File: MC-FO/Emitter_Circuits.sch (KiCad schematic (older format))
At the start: 9 parts, among them U27 74ACT08SCX, U28 IFE98

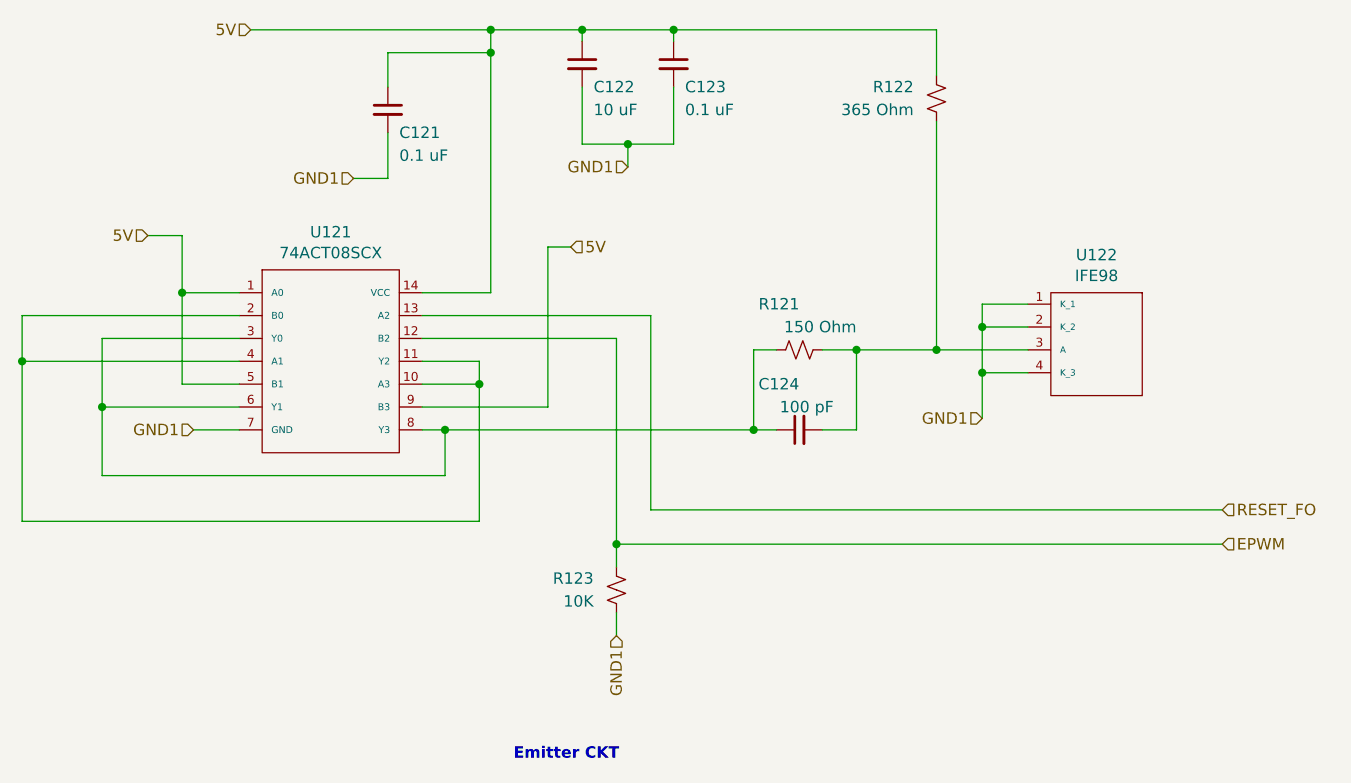
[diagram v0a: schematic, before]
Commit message: changed status1 to output of detector
reassigned footprint of 550 LED
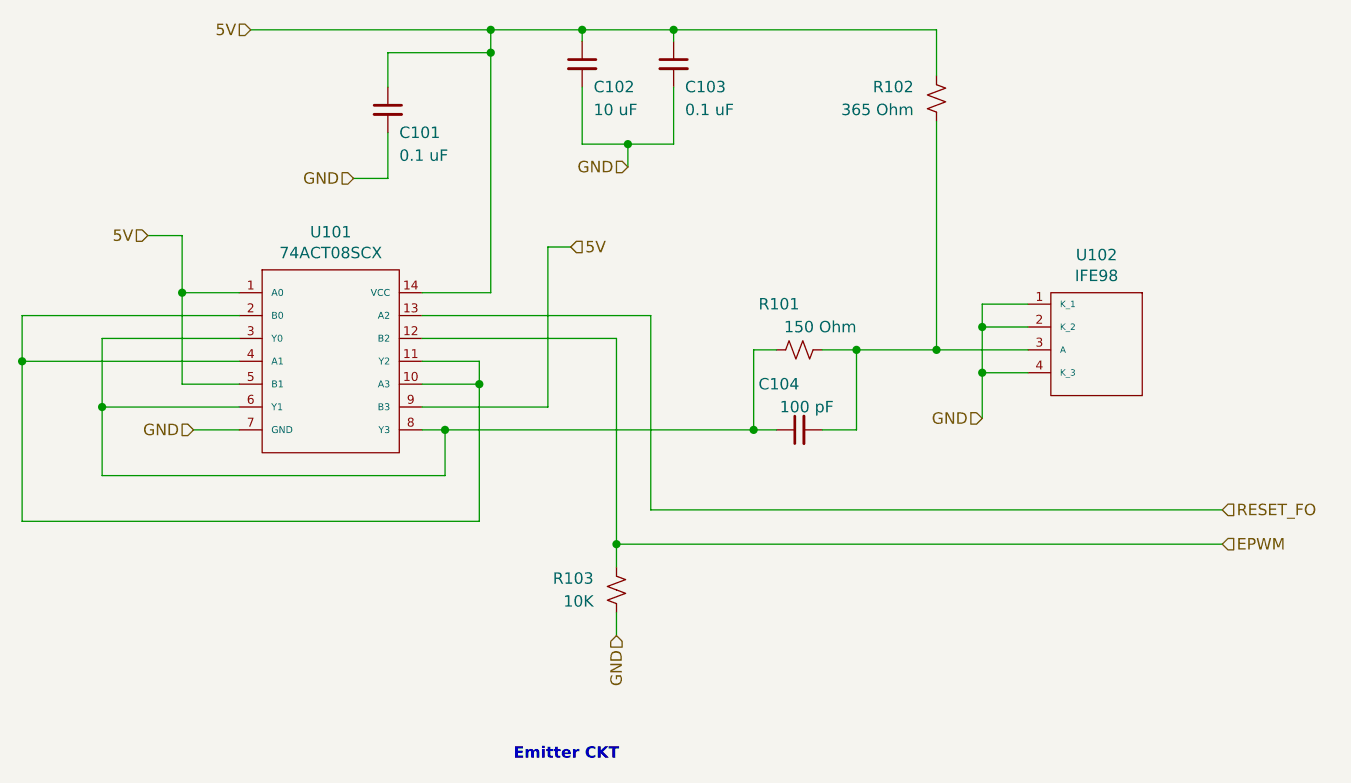
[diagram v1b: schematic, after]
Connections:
- net GND1 renamed GND
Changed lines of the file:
@@
 $Descr A4 11693 8268
 encoding utf-8
-Sheet 3 10
+Sheet 2 10
 Title ""
 Date ""
@@
 AR Path="/6176CA81/617428A7" Ref="R101"  Part="1"
 AR Path="/6176CAE4/617428A7" Ref="R121"  Part="1"
-F 0 "R121" V 6900 4400 50  0000 L CNN
+F 0 "R101" V 6900 4400 50  0000 L CNN
 F 1 "150 Ohm" V 6800 4150 50  0000 L CNN
 F 2 "Resistor_SMD:R_0603_1608Metric" H 6700 4400 50  0001 C CNN
@@
 AR Path="/6176CA81/61748E58" Ref="C104"  Part="1"
 AR Path="/6176CAE4/61748E58" Ref="C124"  Part="1"
-F 0 "C124" V 6900 4750 50  0000 L CNN
+F 0 "C104" V 6900 4750 50  0000 L CNN
 F 1 "100 pF" V 6800 4600 50  0000 L CNN
 F 2 "Capacitor_SMD:C_0603_1608Metric" H 6700 4750 50  0001 C CNN
@@
 AR Path="/6176CA81/6178E7F7" Ref="R102"  Part="1"
 AR Path="/6176CAE4/6178E7F7" Ref="R122"  Part="1"
-F 0 "R122" H 7400 3250 50  0000 L CNN
+F 0 "R102" H 7400 3250 50  0000 L CNN
 F 1 "365 Ohm" H 7400 3350 50  0000 L CNN
 F 2 "Resistor_SMD:R_0603_1608Metric" H 7300 3300 50  0001 C CNN
@@
 AR Path="/6176CA81/6171F0C9" Ref="C101"  Part="1"
 AR Path="/6176CAE4/6171F0C9" Ref="C121"  Part="1"
-F 0 "C121" H 4950 3250 50  0000 L CNN
+F 0 "C101" H 4950 3250 50  0000 L CNN
 F 1 "0.1 uF" H 4950 3150 50  0000 L CNN
 F 2 "Capacitor_SMD:C_0603_1608Metric" H 4900 3350 50  0001 C CNN
@@
 AR Path="/6176CA81/61733718" Ref="C103"  Part="1"
 AR Path="/6176CAE4/61733718" Ref="C123"  Part="1"
-F 0 "C123" H 6200 3050 50  0000 L CNN
+F 0 "C103" H 6200 3050 50  0000 L CNN
 F 1 "0.1 uF" H 6200 2950 50  0000 L CNN
 F 2 "Capacitor_SMD:C_0603_1608Metric" H 6150 3150 50  0001 C CNN
@@
 AR Path="/6176CA81/61730A88" Ref="C102"  Part="1"
 AR Path="/6176CAE4/61730A88" Ref="C122"  Part="1"
-F 0 "C122" H 5800 3050 50  0000 L CNN
+F 0 "C102" H 5800 3050 50  0000 L CNN
 F 1 "10 uF" H 5800 2950 50  0000 L CNN
 F 2 "Capacitor_SMD:C_0603_1608Metric" H 5750 3150 50  0001 C CNN
@@
 5V
 Text HLabel 7500 4700 0    50   Input ~ 0
-GND1
+GND
 Wire Wire Line
 	4300 3000 5350 3000
@@
 AR Path="/6176CA81/61804FDE" Ref="U101"  Part="1"
 AR Path="/6176CAE4/61804FDE" Ref="U121"  Part="1"
-F 0 "U121" H 4650 4115 50  0000 C CNN
+F 0 "U101" H 4650 4115 50  0000 C CNN
 F 1 "74ACT08SCX" H 4650 4024 50  0000 C CNN
 F 2 "Package_SO:SOIC-14_3.9x8.7mm_P1.27mm" H 4650 4000 50  0001 C CNN
@@
 $EndComp
 Text HLabel 4050 4750 0    50   Input ~ 0
-GND1
+GND
 Wire Wire Line
 	5350 3100 5350 4150
@@
 AR Path="/6176CAE4/61778B54" Ref="U122"  Part="1"
 AR Path="/617509F7/61778B54" Ref="U42"  Part="1"
-F 0 "U122" H 8000 4215 50  0000 C CNN
+F 0 "U102" H 8000 4215 50  0000 C CNN
 F 1 "IFE98" H 8000 4124 50  0000 C CNN
 F 2 "Footprints_MC-FO:IFE98" H 8000 4100 50  0001 C CNN
@@
 	5950 3500 6150 3500
 Text HLabel 5950 3600 0    50   Input ~ 0
-GND1
+GND
 Text HLabel 4750 3650 0    50   Input ~ 0
-GND1
+GND
 Wire Wire Line
 	4750 3650 4900 3650
@@
 AR Path="/6176CA81/617DC24B" Ref="R103"  Part="1"
 AR Path="/6176CAE4/617DC24B" Ref="R123"  Part="1"
-F 0 "R123" H 6000 5400 50  0000 L CNN
+F 0 "R103" H 6000 5400 50  0000 L CNN
 F 1 "10K" H 6000 5500 50  0000 L CNN
 F 2 "Resistor_SMD:R_0603_1608Metric" H 5900 5450 50  0001 C CNN
@@
 $EndComp
 Text HLabel 5900 5650 3    50   Input ~ 0
-GND1
+GND
 Wire Wire Line
 	5900 5250 5900 5350

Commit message: DSP schem, FO schem, and FO layout changes
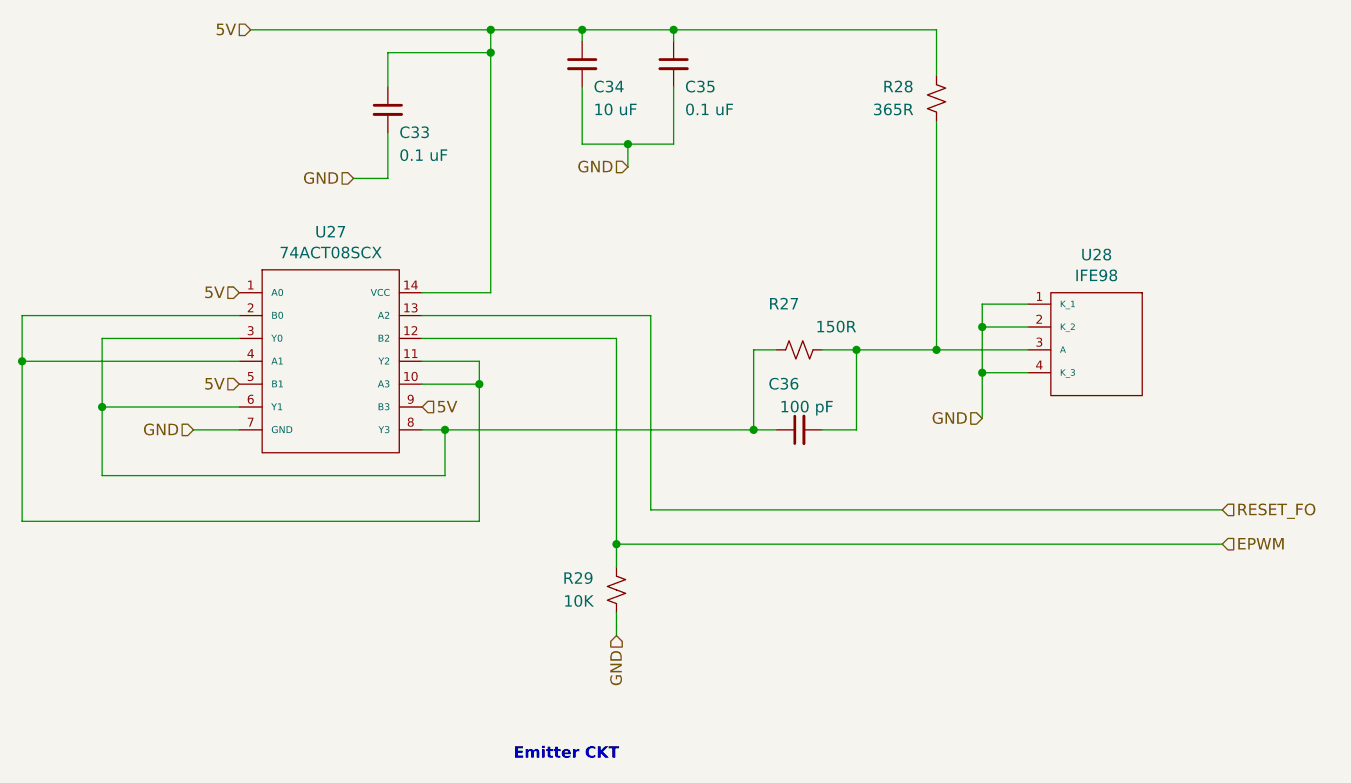
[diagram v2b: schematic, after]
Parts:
- R27: value 150 Ohm -> 150R
- R28: value 365 Ohm -> 365R
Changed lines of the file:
@@
 $Descr A4 11693 8268
 encoding utf-8
-Sheet 2 10
+Sheet 4 10
 Title ""
 Date ""
@@
 AR Path="/6176CA81/617428A7" Ref="R101"  Part="1"
 AR Path="/6176CAE4/617428A7" Ref="R121"  Part="1"
-F 0 "R101" V 6900 4400 50  0000 L CNN
-F 1 "150 Ohm" V 6800 4150 50  0000 L CNN
+F 0 "R27" V 6900 4400 50  0000 L CNN
+F 1 "150R" V 6800 4150 50  0000 L CNN
 F 2 "Resistor_SMD:R_0603_1608Metric" H 6700 4400 50  0001 C CNN
 F 3 "~" H 6700 4400 50  0001 C CNN
@@
 AR Path="/6176CA81/61748E58" Ref="C104"  Part="1"
 AR Path="/6176CAE4/61748E58" Ref="C124"  Part="1"
-F 0 "C104" V 6900 4750 50  0000 L CNN
+F 0 "C36" V 6900 4750 50  0000 L CNN
 F 1 "100 pF" V 6800 4600 50  0000 L CNN
 F 2 "Capacitor_SMD:C_0603_1608Metric" H 6700 4750 50  0001 C CNN
@@
 AR Path="/6176CA81/6178E7F7" Ref="R102"  Part="1"
 AR Path="/6176CAE4/6178E7F7" Ref="R122"  Part="1"
-F 0 "R102" H 7400 3250 50  0000 L CNN
-F 1 "365 Ohm" H 7400 3350 50  0000 L CNN
+F 0 "R28" H 7400 3250 50  0000 L CNN
+F 1 "365R" H 7400 3350 50  0000 L CNN
 F 2 "Resistor_SMD:R_0603_1608Metric" H 7300 3300 50  0001 C CNN
 F 3 "~" H 7300 3300 50  0001 C CNN
@@
 AR Path="/6176CA81/6171F0C9" Ref="C101"  Part="1"
 AR Path="/6176CAE4/6171F0C9" Ref="C121"  Part="1"
-F 0 "C101" H 4950 3250 50  0000 L CNN
+F 0 "C33" H 4950 3250 50  0000 L CNN
 F 1 "0.1 uF" H 4950 3150 50  0000 L CNN
 F 2 "Capacitor_SMD:C_0603_1608Metric" H 4900 3350 50  0001 C CNN
@@
 AR Path="/6176CA81/61733718" Ref="C103"  Part="1"
 AR Path="/6176CAE4/61733718" Ref="C123"  Part="1"
-F 0 "C103" H 6200 3050 50  0000 L CNN
+F 0 "C35" H 6200 3050 50  0000 L CNN
 F 1 "0.1 uF" H 6200 2950 50  0000 L CNN
 F 2 "Capacitor_SMD:C_0603_1608Metric" H 6150 3150 50  0001 C CNN
@@
 AR Path="/6176CA81/61730A88" Ref="C102"  Part="1"
 AR Path="/6176CAE4/61730A88" Ref="C122"  Part="1"
-F 0 "C102" H 5800 3050 50  0000 L CNN
+F 0 "C34" H 5800 3050 50  0000 L CNN
 F 1 "10 uF" H 5800 2950 50  0000 L CNN
 F 2 "Capacitor_SMD:C_0603_1608Metric" H 5750 3150 50  0001 C CNN
@@
 AR Path="/6176CA81/61804FDE" Ref="U101"  Part="1"
 AR Path="/6176CAE4/61804FDE" Ref="U121"  Part="1"
-F 0 "U101" H 4650 4115 50  0000 C CNN
+F 0 "U27" H 4650 4115 50  0000 C CNN
 F 1 "74ACT08SCX" H 4650 4024 50  0000 C CNN
 F 2 "Package_SO:SOIC-14_3.9x8.7mm_P1.27mm" H 4650 4000 50  0001 C CNN
@@
 AR Path="/6176CAE4/61778B54" Ref="U122"  Part="1"
 AR Path="/617509F7/61778B54" Ref="U42"  Part="1"
-F 0 "U102" H 8000 4215 50  0000 C CNN
+F 0 "U28" H 8000 4215 50  0000 C CNN
 F 1 "IFE98" H 8000 4124 50  0000 C CNN
 F 2 "Footprints_MC-FO:IFE98" H 8000 4100 50  0001 C CNN
@@
 Wire Wire Line
 	3300 4250 4250 4250
-Text HLabel 3850 3900 0    50   Input ~ 0
+Text HLabel 4250 4150 0    50   Input ~ 0
 5V
-Text HLabel 5700 3950 2    50   Input ~ 0
+Text HLabel 5050 4650 2    50   Input ~ 0
 5V
-Wire Wire Line
-	5700 3950 5600 3950
-Wire Wire Line
-	5600 3950 5600 4650
-Wire Wire Line
-	5600 4650 5050 4650
-Wire Wire Line
-	3850 3900 4000 3900
-Wire Wire Line
-	4000 3900 4000 4150
-Wire Wire Line
-	4000 4550 4250 4550
-Wire Wire Line
-	4000 4150 4250 4150
-Connection ~ 4000 4150
-Wire Wire Line
-	4000 4150 4000 4550
 Wire Wire Line
 	3300 4450 4250 4450
@@
 AR Path="/6176CA81/617DC24B" Ref="R103"  Part="1"
 AR Path="/6176CAE4/617DC24B" Ref="R123"  Part="1"
-F 0 "R103" H 6000 5400 50  0000 L CNN
+F 0 "R29" H 6000 5400 50  0000 L CNN
 F 1 "10K" H 6000 5500 50  0000 L CNN
 F 2 "Resistor_SMD:R_0603_1608Metric" H 5900 5450 50  0001 C CNN
@@
 Wire Wire Line
 	5900 5550 5900 5650
+Text HLabel 4250 4550 0    50   Input ~ 0
+5V
 $EndSCHEMATC

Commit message: Add files via upload
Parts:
- added TP14: TestPoint, TestPoint:TestPoint_Pad_D2.0mm, symbol Connector:TestPoint
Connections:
- net EPWM: now also TP14.1
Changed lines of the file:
@@
 $Descr A4 11693 8268
 encoding utf-8
-Sheet 4 10
+Sheet 4 11
 Title ""
 Date ""
@@
 AR Path="/6176CA81/617428A7" Ref="R101"  Part="1"
 AR Path="/6176CAE4/617428A7" Ref="R121"  Part="1"
-F 0 "R27" V 6900 4400 50  0000 L CNN
+F 0 "R81" V 6900 4400 50  0000 L CNN
 F 1 "150R" V 6800 4150 50  0000 L CNN
 F 2 "Resistor_SMD:R_0603_1608Metric" H 6700 4400 50  0001 C CNN
@@
 AR Path="/6176CA81/61748E58" Ref="C104"  Part="1"
 AR Path="/6176CAE4/61748E58" Ref="C124"  Part="1"
-F 0 "C36" V 6900 4750 50  0000 L CNN
+F 0 "C84" V 6900 4750 50  0000 L CNN
 F 1 "100 pF" V 6800 4600 50  0000 L CNN
 F 2 "Capacitor_SMD:C_0603_1608Metric" H 6700 4750 50  0001 C CNN
@@
 AR Path="/6176CA81/6178E7F7" Ref="R102"  Part="1"
 AR Path="/6176CAE4/6178E7F7" Ref="R122"  Part="1"
-F 0 "R28" H 7400 3250 50  0000 L CNN
+F 0 "R82" H 7400 3250 50  0000 L CNN
 F 1 "365R" H 7400 3350 50  0000 L CNN
 F 2 "Resistor_SMD:R_0603_1608Metric" H 7300 3300 50  0001 C CNN
@@
 AR Path="/6176CA81/6171F0C9" Ref="C101"  Part="1"
 AR Path="/6176CAE4/6171F0C9" Ref="C121"  Part="1"
-F 0 "C33" H 4950 3250 50  0000 L CNN
+F 0 "C81" H 4950 3250 50  0000 L CNN
 F 1 "0.1 uF" H 4950 3150 50  0000 L CNN
 F 2 "Capacitor_SMD:C_0603_1608Metric" H 4900 3350 50  0001 C CNN
@@
 AR Path="/6176CA81/61733718" Ref="C103"  Part="1"
 AR Path="/6176CAE4/61733718" Ref="C123"  Part="1"
-F 0 "C35" H 6200 3050 50  0000 L CNN
+F 0 "C83" H 6200 3050 50  0000 L CNN
 F 1 "0.1 uF" H 6200 2950 50  0000 L CNN
 F 2 "Capacitor_SMD:C_0603_1608Metric" H 6150 3150 50  0001 C CNN
@@
 AR Path="/6176CA81/61730A88" Ref="C102"  Part="1"
 AR Path="/6176CAE4/61730A88" Ref="C122"  Part="1"
-F 0 "C34" H 5800 3050 50  0000 L CNN
+F 0 "C82" H 5800 3050 50  0000 L CNN
 F 1 "10 uF" H 5800 2950 50  0000 L CNN
 F 2 "Capacitor_SMD:C_0603_1608Metric" H 5750 3150 50  0001 C CNN
@@
 $EndComp
 Wire Wire Line
-	5900 5250 8550 5250
+	5900 5250 7475 5250
 Text HLabel 8550 5250 2    50   Input ~ 0
 EPWM
@@
 AR Path="/6176CA81/61804FDE" Ref="U101"  Part="1"
 AR Path="/6176CAE4/61804FDE" Ref="U121"  Part="1"
-F 0 "U27" H 4650 4115 50  0000 C CNN
+F 0 "U81" H 4650 4115 50  0000 C CNN
 F 1 "74ACT08SCX" H 4650 4024 50  0000 C CNN
 F 2 "Package_SO:SOIC-14_3.9x8.7mm_P1.27mm" H 4650 4000 50  0001 C CNN
@@
 AR Path="/6176CAE4/61778B54" Ref="U122"  Part="1"
 AR Path="/617509F7/61778B54" Ref="U42"  Part="1"
-F 0 "U28" H 8000 4215 50  0000 C CNN
+F 0 "U82" H 8000 4215 50  0000 C CNN
 F 1 "IFE98" H 8000 4124 50  0000 C CNN
 F 2 "Footprints_MC-FO:IFE98" H 8000 4100 50  0001 C CNN
@@
 AR Path="/6176CA81/617DC24B" Ref="R103"  Part="1"
 AR Path="/6176CAE4/617DC24B" Ref="R123"  Part="1"
-F 0 "R29" H 6000 5400 50  0000 L CNN
+F 0 "R83" H 6000 5400 50  0000 L CNN
 F 1 "10K" H 6000 5500 50  0000 L CNN
 F 2 "Resistor_SMD:R_0603_1608Metric" H 5900 5450 50  0001 C CNN
@@
 Text HLabel 4250 4550 0    50   Input ~ 0
 5V
+$Comp
+L Connector:TestPoint TP14
+U 1 1 623D825D
+P 7475 5250
+AR Path="/61717EAF/623D825D" Ref="TP14"  Part="1"
+AR Path="/6176CA81/623D825D" Ref="TP12"  Part="1"
+AR Path="/6176CAE4/623D825D" Ref="TP13"  Part="1"
+AR Path="/617509F7/623D825D" Ref="TP15"  Part="1"
+AR Path="/61750A2A/623D825D" Ref="TP16"  Part="1"
+AR Path="/6176CA10/623D825D" Ref="TP20"  Part="1"
+F 0 "TP20" H 7417 5276 50  0000 R CNN
+F 1 "TestPoint" H 7417 5367 50  0000 R CNN
+F 2 "TestPoint:TestPoint_Pad_D2.0mm" H 7675 5250 50  0001 C CNN
+F 3 "~" H 7675 5250 50  0001 C CNN
+	1    7475 5250
+	-1   0    0    1
+$EndComp
+Connection ~ 7475 5250
+Wire Wire Line
+	7475 5250 8550 5250
 $EndSCHEMATC
